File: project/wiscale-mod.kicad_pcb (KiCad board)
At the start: 2 copper layers, 100 x 50 mm, 44 parts, among them J5 cell, J6 DS18B20, J7 DS18B20, Q1 AO3401A, Q2 AO3401A, SW1 SW_SPDT, U1 BMS_USB_LiPo_Charger, U2 ADC_HX711, U3 WeMos_D1_mini, U4 TPL5110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

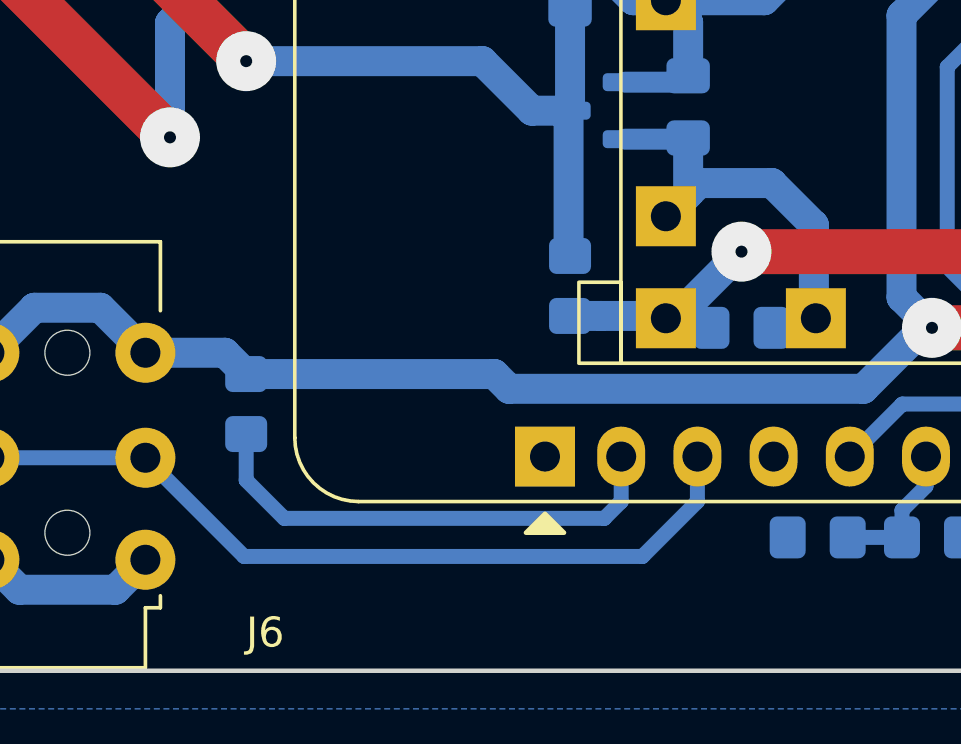
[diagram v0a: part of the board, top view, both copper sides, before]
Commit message: moving thermometer from D0 to D5. fixes #1
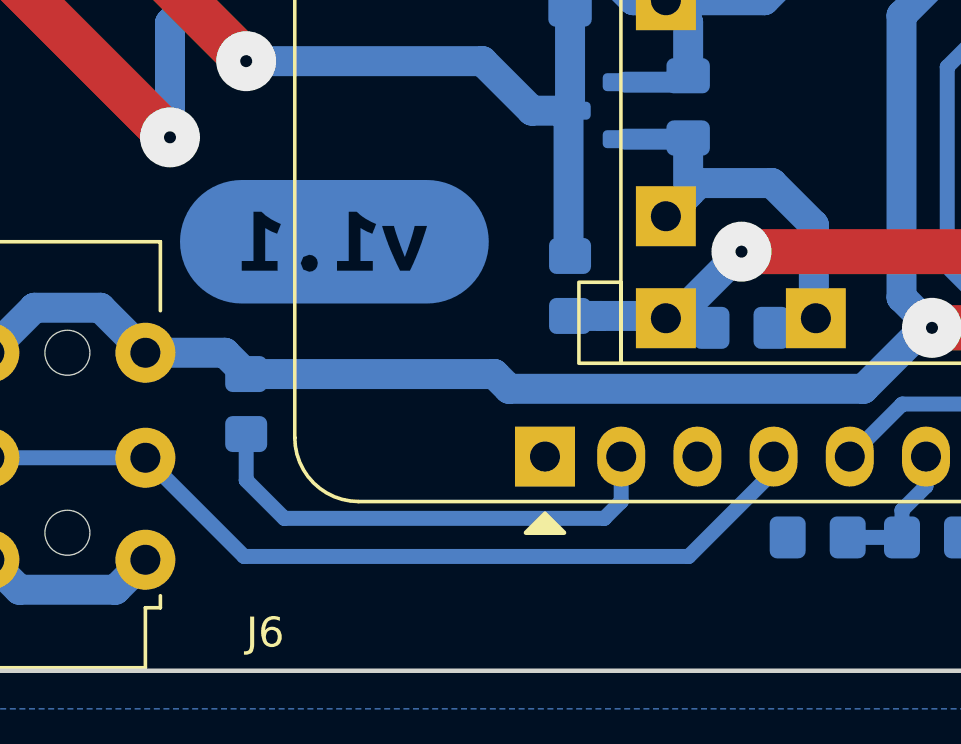
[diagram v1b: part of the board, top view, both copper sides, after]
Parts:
- added kibuzzard-634A7925: G***, kibuzzard-634A7925, B.Cu at (165.5, 111.9)
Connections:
- U3 pad 3: /1w -> unconnected-(U3-Pad3)
- U3 pad 4: unconnected-(U3-Pad4) -> /1w
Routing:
- net /1w: track 38.1 -> 40.1 mm
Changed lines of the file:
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@@
   (net 31 "/_A0")
   (net 32 "Net-(R11-Pad2)")
-  (net 33 "unconnected-(U3-Pad4)")
+  (net 33 "unconnected-(U3-Pad3)")
   (net 34 "/_delay")
   (net 35 "Net-(R8-Pad1)")
@@
       (net 31 "/_A0") (pinfunction "A0") (pintype "input"))
     (pad "3" thru_hole oval (at 0 5.08 90) (size 2 1.6) (drill 1) (layers *.Cu *.Mask)
-      (net 9 "/1w") (pinfunction "D0") (pintype "bidirectional"))
+      (net 33 "unconnected-(U3-Pad3)") (pinfunction "D0") (pintype "bidirectional+no_connect"))
     (pad "4" thru_hole oval (at 0 7.62 90) (size 2 1.6) (drill 1) (layers *.Cu *.Mask)
-      (net 33 "unconnected-(U3-Pad4)") (pinfunction "SCK/D5") (pintype "bidirectional+no_connect"))
+      (net 9 "/1w") (pinfunction "SCK/D5") (pintype "bidirectional"))
     (pad "5" thru_hole oval (at 0 10.16 90) (size 2 1.6) (drill 1) (layers *.Cu *.Mask)
       (net 15 "/mcu_done") (pinfunction "MISO/D6") (pintype "bidirectional"))
@@
     )
   )
+  (footprint "kibuzzard-634A7925" (layer "B.Cu")
+    (at 165.5 111.9 180)
+    (descr "Generated with KiBuzzard")
+    (tags "kb_params=eyJBbGlnbm1lbnRDaG9pY2UiOiAiQ2VudGVyIiwgIkNhcExlZnRDaG9pY2UiOiAiKCIsICJDYXBSaWdodENob2ljZSI6ICIpIiwgIkZvbnRDb21ib0JveCI6ICJVYnVudHVNb25vLUIiLCAiSGVpZ2h0Q3RybCI6ICIyIiwgIkxheWVyQ29tYm9Cb3giOiAiRi5DdSIsICJNdWx0aUxpbmVUZXh0IjogInYxLjEiLCAiUGFkZGluZ0JvdHRvbUN0cmwiOiAiOCIsICJQYWRkaW5nTGVmdEN0cmwiOiAiMCIsICJQYWRkaW5nUmlnaHRDdHJsIjogIjAiLCAiUGFkZGluZ1RvcEN0cmwiOiAiOCIsICJXaWR0aEN0cmwiOiAiIn0=")
+    (attr board_only exclude_from_pos_files exclude_from_bom)
+    (fp_text reference "kibuzzard-634A7925" (at 0 5.106458) (layer "B.SilkS") hide
+      (effects (font (size 0 0)) (justify mirror))
+    )
+    (fp_text value "G***" (at 0 -5.106458) (layer "B.SilkS") hide
+      (effects (font (size 0 0)) (justify mirror))
+    )
+    (fp_poly (pts
+        (xy -3.087688 2.058458)
+        (xy -3.087952 2.058458)
+        (xy -3.289716 2.048546)
+        (xy -3.489537 2.018906)
+        (xy -3.685491 1.969822)
+        (xy -3.87569 1.901768)
+        (xy -4.058303 1.815398)
+        (xy -4.23157 1.711546)
+        (xy -4.393824 1.59121)
+        (xy -4.543502 1.45555)
+        (xy -4.679162 1.305872)
+        (xy -4.799498 1.143618)
+        (xy -4.90335 0.970351)
+        (xy -4.98972 0.787738)
+        (xy -5.057774 0.597539)
+        (xy -5.106858 0.401585)
+        (xy -5.136498 0.201764)
+        (xy -5.14641 0)
+        (xy -5.136498 -0.201764)
+        (xy -5.106858 -0.401585)
+        (xy -5.057774 -0.597539)
+        (xy -4.98972 -0.787738)
+        (xy -4.90335 -0.970351)
+        (xy -4.799498 -1.143618)
+        (xy -4.679162 -1.305872)
+        (xy -4.543502 -1.45555)
+        (xy -4.393824 -1.59121)
+        (xy -4.23157 -1.711546)
+        (xy -4.058303 -1.815398)
+        (xy -3.87569 -1.901768)
+        (xy -3.685491 -1.969822)
+        (xy -3.489537 -2.018906)
+        (xy -3.289716 -2.048546)
+        (xy -3.087952 -2.058458)
+        (xy -3.087688 -2.058458)
+        (xy -2.516188 -2.058458)
+        (xy -2.516188 -0.9652)
+        (xy -2.611967 -0.766057)
+        (xy -2.708804 -0.545394)
+        (xy -2.8067 -0.303213)
+        (xy -2.879626 -0.109041)
+        (xy -2.950766 0.094059)
+        (xy -3.02012 0.30609)
+        (xy -3.087688 0.52705)
+        (xy -2.678113 0.52705)
+        (xy -2.646759 0.402431)
+        (xy -2.60985 0.269875)
+        (xy -2.568972 0.132953)
+        (xy -2.525713 -0.004763)
+        (xy -2.480866 -0.140891)
+        (xy -2.435225 -0.27305)
+        (xy -2.347913 -0.511175)
+        (xy -2.255838 -0.27305)
+        (xy -2.205434 -0.140891)
+        (xy -2.155825 -0.004763)
+        (xy -2.107406 0.132953)
+        (xy -2.060575 0.269875)
+        (xy -2.018903 0.402431)
+        (xy -1.985963 0.52705)
+        (xy -1.589088 0.52705)
+        (xy -1.657548 0.30609)
+        (xy -1.729581 0.094059)
+        (xy -1.805186 -0.109041)
+        (xy -1.884363 -0.303213)
+        (xy -1.990196 -0.545394)
+        (xy -2.091796 -0.766057)
+        (xy -2.189163 -0.9652)
+        (xy -2.516188 -0.9652)
+        (xy -2.516188 -2.058458)
+        (xy -0.087313 -2.058458)
+        (xy -0.087313 -0.9652)
+        (xy -1.281113 -0.9652)
+        (xy -1.281113 -0.64135)
+        (xy -0.868363 -0.64135)
+        (xy -0.868363 0.4572)
+        (xy -1.071563 0.344487)
+        (xy -1.265238 0.2667)
+        (xy -1.392238 0.59055)
+        (xy -1.227138 0.663575)
+        (xy -1.049338 0.762)
+        (xy -0.881063 0.8763)
+        (xy -0.744538 1.000125)
+        (xy -0.477838 1.000125)
+        (xy -0.477838 -0.64135)
+        (xy -0.087313 -0.64135)
+        (xy -0.087313 -0.9652)
+        (xy -0.087313 -2.058458)
+        (xy 0.839787 -2.058458)
+        (xy 0.839787 -1.000125)
+        (xy 0.731837 -0.981075)
+        (xy 0.64135 -0.925513)
+        (xy 0.57785 -0.836613)
+        (xy 0.554037 -0.714375)
+        (xy 0.57785 -0.595313)
+        (xy 0.64135 -0.508)
+        (xy 0.731837 -0.454025)
+        (xy 0.839787 -0.434975)
+        (xy 1.036637 -0.508)
+        (xy 1.122362 -0.714375)
+        (xy 1.036637 -0.9271)
+        (xy 0.839787 -1.000125)
+        (xy 0.839787 -2.058458)
+        (xy 3.087687 -2.058458)
+        (xy 3.087687 -0.9652)
+        (xy 1.893887 -0.9652)
+        (xy 1.893887 -0.64135)
+        (xy 2.306637 -0.64135)
+        (xy 2.306637 0.4572)
+        (xy 2.103437 0.344487)
+        (xy 1.909762 0.2667)
+        (xy 1.782762 0.59055)
+        (xy 1.947862 0.663575)
+        (xy 2.125662 0.762)
+        (xy 2.293937 0.8763)
+        (xy 2.430462 1.000125)
+        (xy 2.697162 1.000125)
+        (xy 2.697162 -0.64135)
+        (xy 3.087687 -0.64135)
+        (xy 3.087687 -0.9652)
+        (xy 3.087687 -2.058458)
+        (xy 3.087952 -2.058458)
+        (xy 3.289716 -2.048546)
+        (xy 3.489537 -2.018906)
+        (xy 3.685491 -1.969822)
+        (xy 3.87569 -1.901768)
+        (xy 4.058303 -1.815398)
+        (xy 4.23157 -1.711546)
+        (xy 4.393824 -1.59121)
+        (xy 4.543502 -1.45555)
+        (xy 4.679162 -1.305872)
+        (xy 4.799498 -1.143618)
+        (xy 4.90335 -0.970351)
+        (xy 4.98972 -0.787738)
+        (xy 5.057774 -0.597539)
+        (xy 5.106858 -0.401585)
+        (xy 5.136498 -0.201764)
+        (xy 5.14641 0)
+        (xy 5.136498 0.201764)
+        (xy 5.106858 0.401585)
+        (xy 5.057774 0.597539)
+        (xy 4.98972 0.787738)
+        (xy 4.90335 0.970351)
+        (xy 4.799498 1.143618)
+        (xy 4.679162 1.305872)
+        (xy 4.543502 1.45555)
+        (xy 4.393824 1.59121)
+        (xy 4.23157 1.711546)
+        (xy 4.058303 1.815398)
+        (xy 3.87569 1.901768)
+        (xy 3.685491 1.969822)
+        (xy 3.489537 2.018906)
+        (xy 3.289716 2.048546)
+        (xy 3.087952 2.058458)
+        (xy 3.087687 2.058458)
+        (xy -3.087688 2.058458)
+      ) (layer "B.Cu") (width 0) (fill solid))
+  )
   (footprint "Resistor_SMD:R_0805_2012Metric_Pad1.20x1.40mm_HandSolder" (layer "B.Cu")
     (at 194.945 79.845)
@@
   (segment (start 111.77 110.95) (end 112.52 110.2) (width 0.5) (layer "B.Cu") (net 8))
   (segment (start 109.6 110.95) (end 111.77 110.95) (width 0.5) (layer "B.Cu") (net 8))
-  (segment (start 175.768 122.39) (end 177.6 120.558) (width 0.5) (layer "B.Cu") (net 9))
+  (segment (start 162.49 122.39) (end 177.31 122.39) (width 0.5) (layer "B.Cu") (net 9))
   (segment (start 145.6 118.141) (end 147.32 116.421) (width 0.5) (layer "B.Cu") (net 9))
+  (segment (start 159.2 119.1) (end 162.49 122.39) (width 0.5) (layer "B.Cu") (net 9))
   (segment (start 151.269 119.1) (end 154 119.1) (width 0.5) (layer "B.Cu") (net 9))
   (segment (start 149.356 116.421) (end 150.114 117.179) (width 0.5) (layer "B.Cu") (net 9))
   (segment (start 150.114 117.179) (end 150.114 117.945) (width 0.5) (layer "B.Cu") (net 9))
+  (segment (start 180.14 119.56) (end 180.14 119.06) (width 0.5) (layer "B.Cu") (net 9))
   (segment (start 147.32 116.421) (end 149.356 116.421) (width 0.5) (layer "B.Cu") (net 9))
-  (segment (start 177.6 120.558) (end 177.6 119.06) (width 0.5) (layer "B.Cu") (net 9))
+  (segment (start 177.31 122.39) (end 180.14 119.56) (width 0.5) (layer "B.Cu") (net 9))
   (segment (start 145.6 118.35) (end 145.6 118.141) (width 0.5) (layer "B.Cu") (net 9))
-  (segment (start 162.49 122.39) (end 175.768 122.39) (width 0.5) (layer "B.Cu") (net 9))
   (segment (start 150.114 117.945) (end 151.269 119.1) (width 0.5) (layer "B.Cu") (net 9))
   (segment (start 154 119.1) (end 159.2 119.1) (width 0.5) (layer "B.Cu") (net 9))
-  (segment (start 159.2 119.1) (end 162.49 122.39) (width 0.5) (layer "B.Cu") (net 9))
   (segment (start 190.722 121.66) (end 192.024 120.358) (width 1) (layer "B.Cu") (net 10))
   (segment (start 192.024 118.961) (end 196.535 114.45) (width 1) (layer "B.Cu") (net 10))
@@
     (connect_pads yes (clearance 0))
     (min_thickness 0.254)
-    (keepout (tracks not_allowed) (vias allowed) (pads allowed) (copperpour not_allowed) (footprints allowed))
+    (keepout (tracks allowed) (vias allowed) (pads allowed) (copperpour not_allowed) (footprints allowed))
     (fill (thermal_gap 0.508) (thermal_bridge_width 0.508))
     (polygon

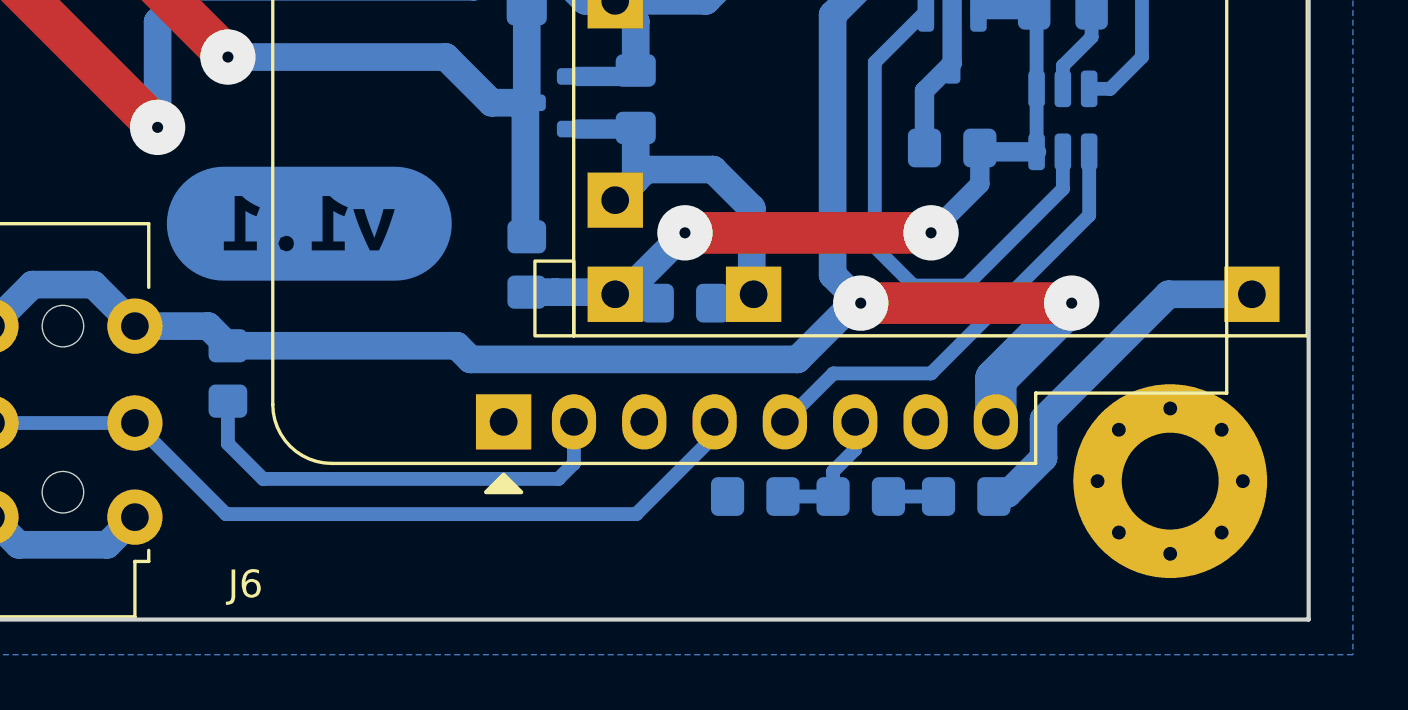
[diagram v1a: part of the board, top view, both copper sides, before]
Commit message: adding pull-down on MCU_DONE pin. fixes #2
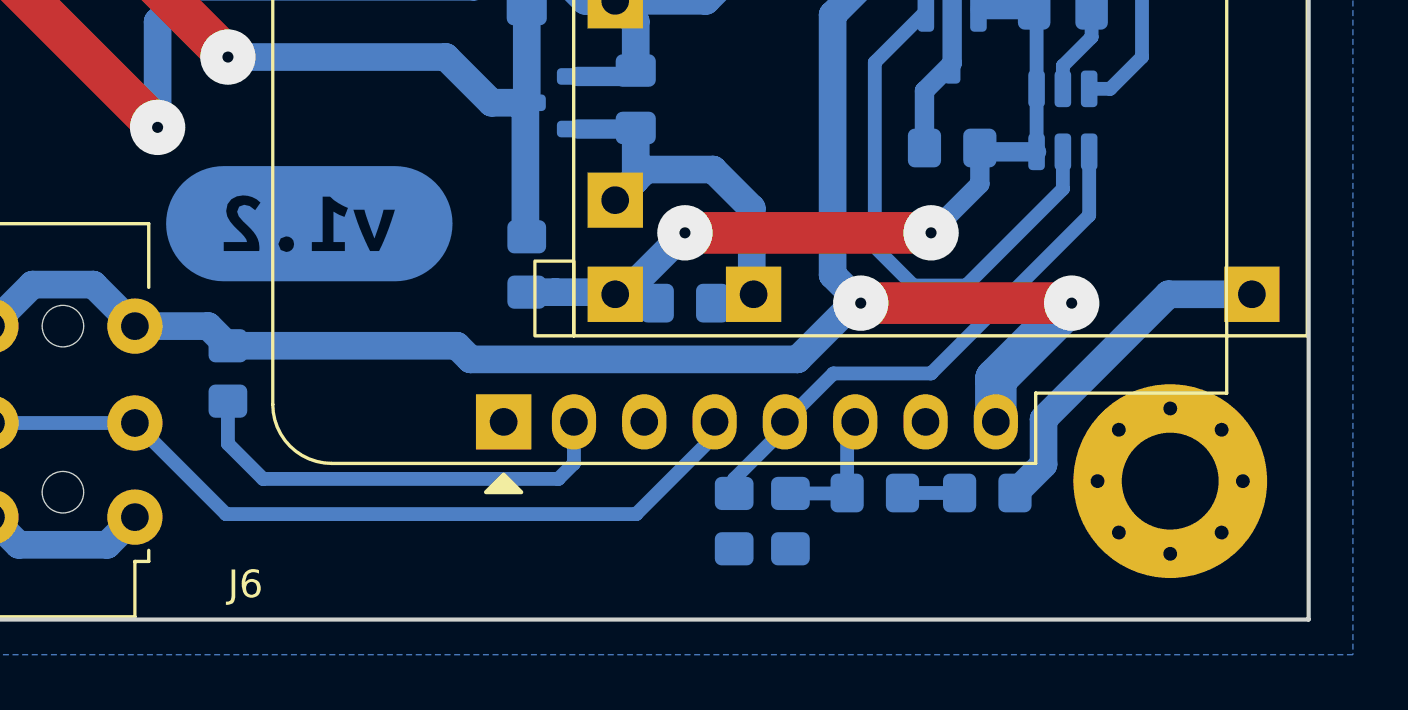
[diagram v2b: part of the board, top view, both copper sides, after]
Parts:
- removed kibuzzard-634A7925: G***, kibuzzard-634A7925
- added R17: 4k7, Resistor_SMD:R_0805_2012Metric_Pad1.20x1.40mm_HandSolder, B.Cu at (180.8, 122.6)
- added kibuzzard-634A7C40: G***, kibuzzard-634A7C40, B.Cu at (165.5, 111.9)
- moved R10 1.55 mm to (182.9, 122.6), turned to 90 degrees
- moved R8 0.77 mm to (190.0, 121.6)
- moved R9 0.52 mm to (185.9, 121.6)
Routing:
- net /mcu_done: track 16.4 -> 19.7 mm

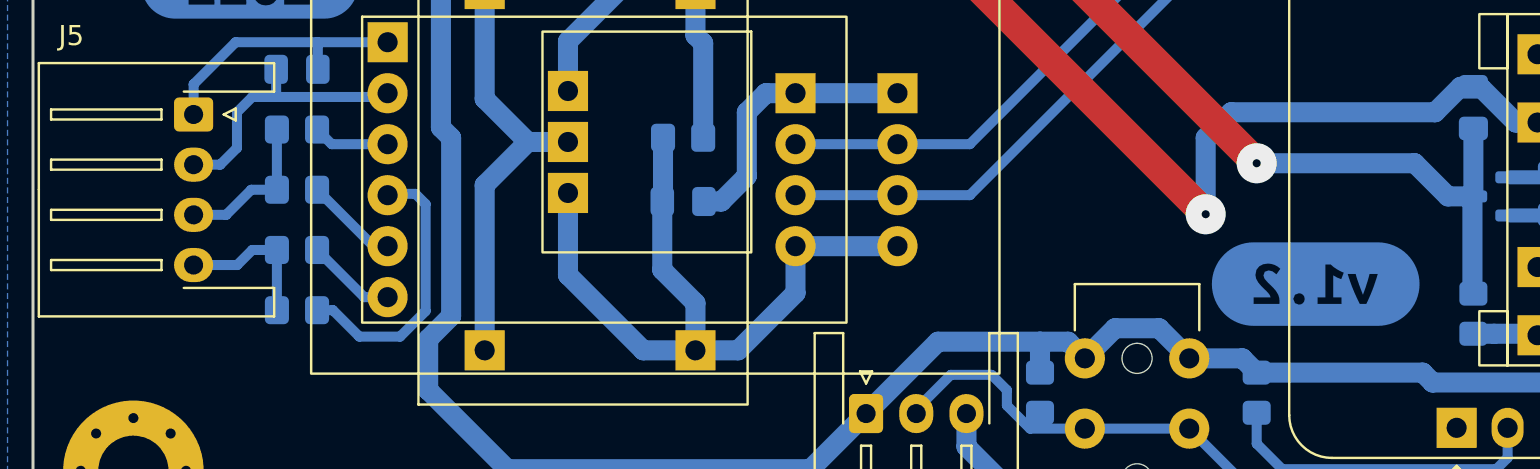
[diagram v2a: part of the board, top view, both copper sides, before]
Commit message: adding caps to ADC input to average out noise
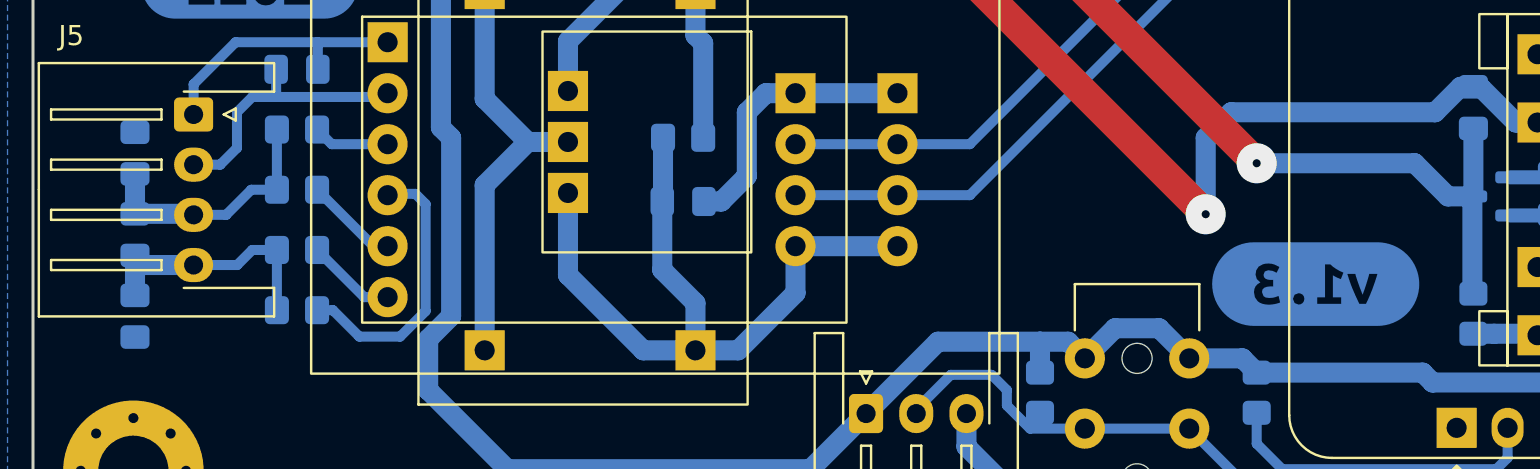
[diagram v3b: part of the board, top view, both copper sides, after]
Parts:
- removed kibuzzard-634A7C40: G***, kibuzzard-634A7C40
- added C10: 100n, Capacitor_SMD:C_0805_2012Metric_Pad1.18x1.45mm_HandSolder, B.Cu at (106.7, 109.4)
- added C11: 100n, Capacitor_SMD:C_0805_2012Metric_Pad1.18x1.45mm_HandSolder, B.Cu at (106.7, 105.4)
- added C9: 100n, Capacitor_SMD:C_0805_2012Metric_Pad1.18x1.45mm_HandSolder, B.Cu at (106.7, 113.5)
- added kibuzzard-6352768B: G***, kibuzzard-6352768B, B.Cu at (165.5, 111.9)
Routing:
- net /A+: track 7.46 -> 12.6 mm
- net /A-: track 7.67 -> 12.6 mm
